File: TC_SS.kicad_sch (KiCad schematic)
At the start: 35 parts, among them Q1 C2M0025120D, Q2 C2M0025120D, Q3 C2M0025120D, Q4 C2M0025120D, U1 IR2184, U2 IR2184, U3 SN74LVC1G14DBV, U4 SN74LVC1G14DBV, U5 NE555D

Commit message: Add more values
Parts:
- D8, D9: value D -> 1n4148
- F1: value Fuse -> 10A
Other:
- moved on the sheet: AE1
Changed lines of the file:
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@@
     (stroke (width 0) (type default))
   )
-  (wire (pts (xy 118.11 166.37) (xy 109.22 166.37))
+  (wire (pts (xy 120.65 166.37) (xy 109.22 166.37))
     (stroke (width 0) (type default))
   )
@@
     (stroke (width 0) (type default))
   )
-  (wire (pts (xy 118.11 165.1) (xy 118.11 166.37))
+  (wire (pts (xy 120.65 165.1) (xy 120.65 166.37))
     (stroke (width 0) (type default))
   )
@@
       (effects (font (size 1.27 1.27)) (justify left))
     )
-    (property "Value" "D" (at 111.76 161.29 90)
+    (property "Value" "1n4148" (at 111.76 161.29 90)
       (effects (font (size 1.27 1.27)) (justify left))
     )
@@
       (effects (font (size 1.27 1.27)))
     )
-    (property "Value" "Fuse" (at 41.91 43.18 90)
+    (property "Value" "10A" (at 41.91 43.18 90)
       (effects (font (size 1.27 1.27)))
     )
@@
       (effects (font (size 1.27 1.27)) (justify left))
     )
-    (property "Value" "D" (at 111.76 173.99 90)
+    (property "Value" "1n4148" (at 111.76 173.99 90)
       (effects (font (size 1.27 1.27)) (justify left))
     )
@@
     )
   )
-  (symbol (lib_id "Device:Antenna") (at 118.11 160.02 0) (unit 1)
-    (in_bom yes) (on_board yes) (dnp no) (fields_autoplaced)
-    (property "Reference" "AE1" (at 120.65 159.385 0)
-      (effects (font (size 1.27 1.27)) (justify left))
-    )
-    (property "Value" "Antenna" (at 120.65 161.925 0)
-      (effects (font (size 1.27 1.27)) (justify left))
-    )
-    (property "Footprint" "" (at 118.11 160.02 0)
-      (effects (font (size 1.27 1.27)) hide)
-    )
-    (property "Datasheet" "~" (at 118.11 160.02 0)
-      (effects (font (size 1.27 1.27)) hide)
-    )
+  (symbol (lib_id "Device:Antenna") (at 120.65 160.02 0) (unit 1)
+    (in_bom yes) (on_board yes) (dnp no) (fields_autoplaced)
+    (property "Reference" "AE1" (at 123.19 159.385 0)
+      (effects (font (size 1.27 1.27)) (justify left))
+    )
+    (property "Value" "Antenna" (at 123.19 161.925 0)
+      (effects (font (size 1.27 1.27)) (justify left))
+    )
+    (property "Footprint" "" (at 120.65 160.02 0)
+      (effects (font (size 1.27 1.27)) hide)
+    )
+    (property "Datasheet" "~" (at 120.65 160.02 0)
+      (effects (font (size 1.27 1.27)) hide)
+    )

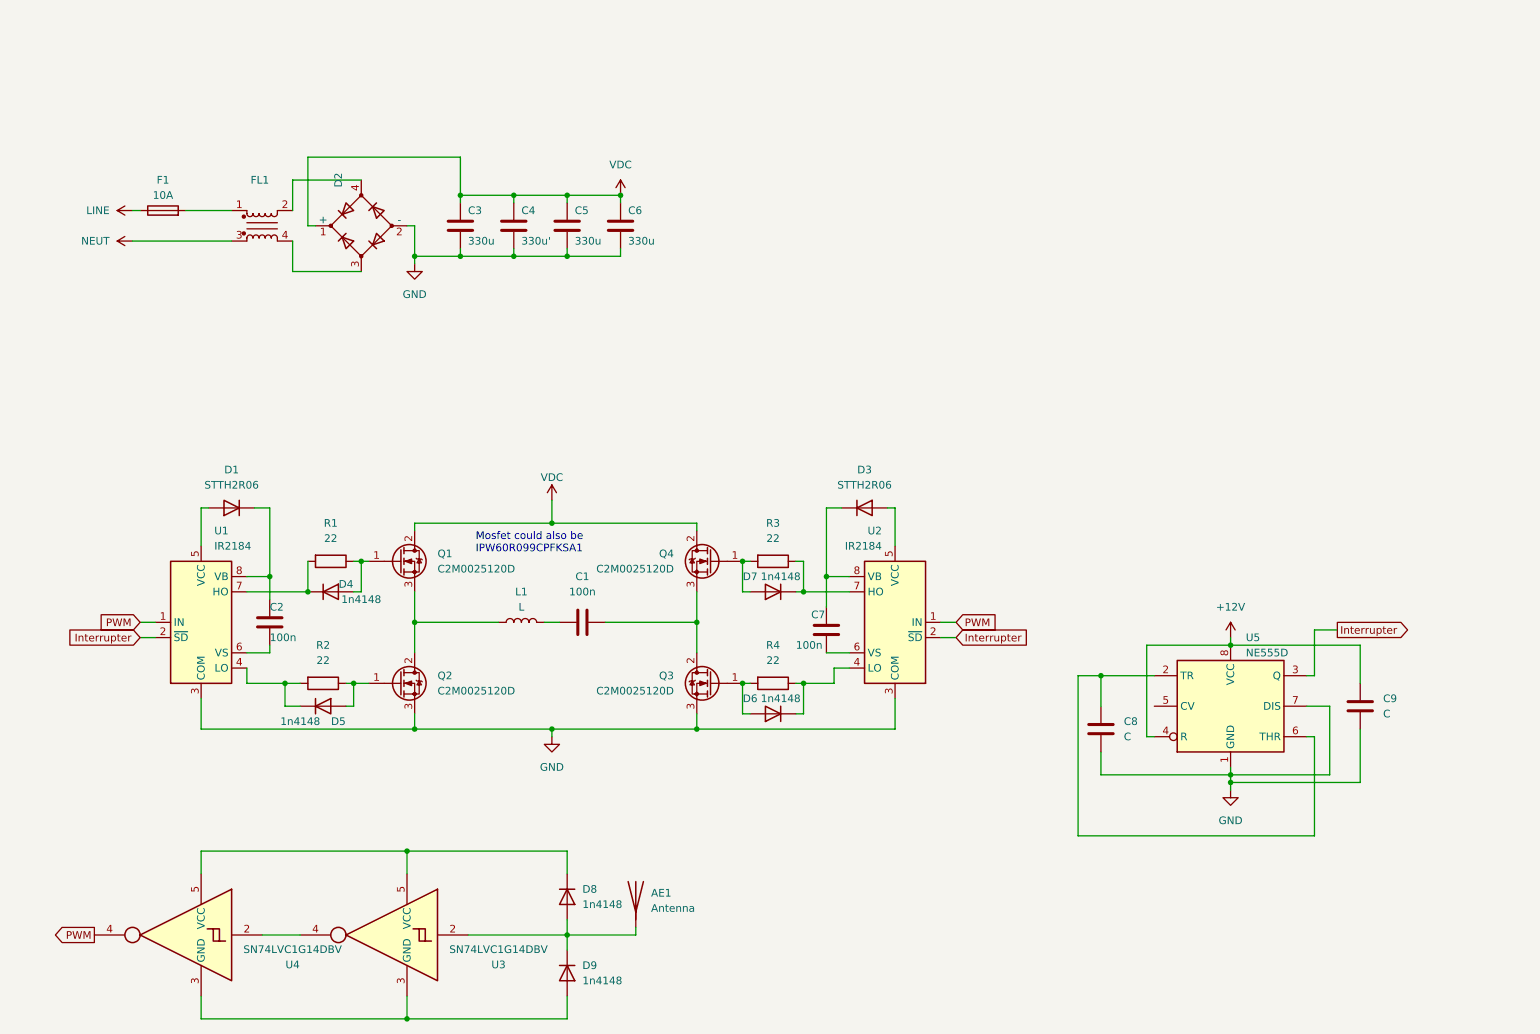
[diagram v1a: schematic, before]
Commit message: Update input driver
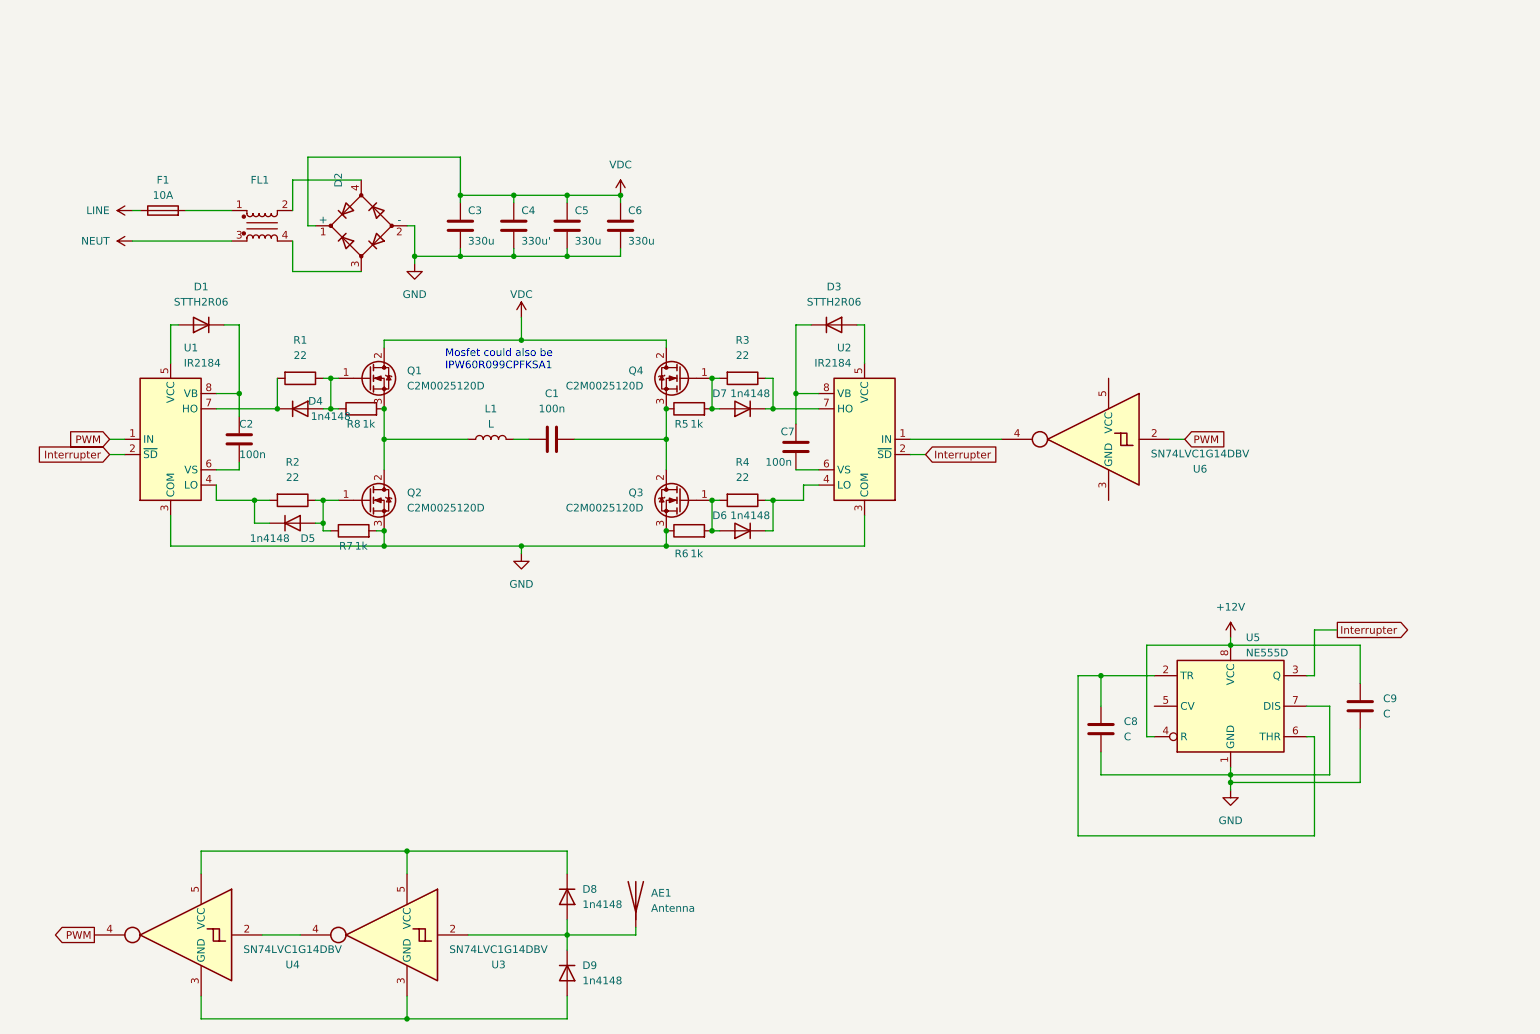
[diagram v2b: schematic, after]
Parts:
- added R5, R6, R7, R8: 1k, Resistor_SMD:R_1206_3216Metric_Pad1.30x1.75mm_HandSolder, symbol Device:R
- added U6: SN74LVC1G14DBV, Package_TO_SOT_SMD:SOT-23-5, symbol 74xGxx:SN74LVC1G14DBV
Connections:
- net GND: now also R6.1, R7.2
- net PWM: now also U6.2; no longer U2.1 (IN)
- net at D4.2 (A), Q1.1 (G), R1.1: now also R8.1
- net at L1.1, Q1.3 (S), Q2.2 (D): now also R8.2
- net at D5.2 (A), Q2.1 (G), R2.1: now also R7.1
- net at D6.2 (A), Q3.1 (G), R4.2: now also R6.2
- net at C1.2, Q3.2 (D), Q4.3 (S): now also R5.1
- net at D7.2 (A), Q4.1 (G), R3.2: now also R5.2
- new net: U2.1 (IN), U6.4
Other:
- moved on the sheet: C1, C2, C7, D1, D3, D4, D5, D6, D7, L1, Q1, Q2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

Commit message: Add more footprints and start board
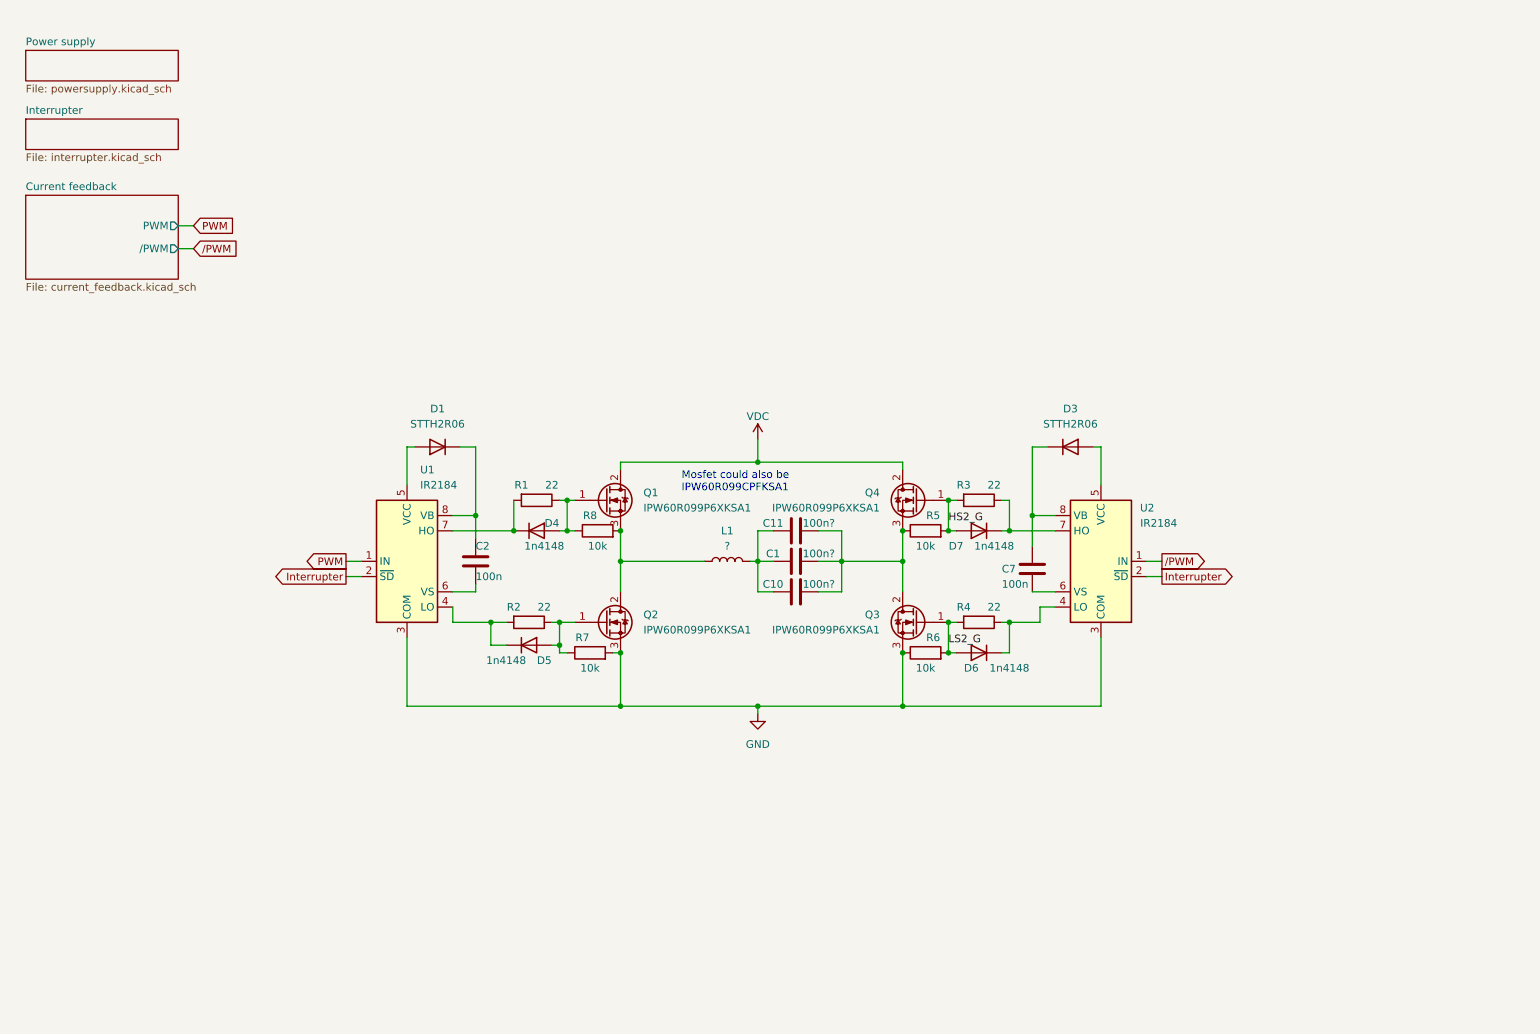
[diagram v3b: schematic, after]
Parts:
- removed AE1: Antenna, symbol Device:Antenna
- removed C3, C5, C6: 330u, Capacitor_SMD:C_0805_2012Metric_Pad1.18x1.45mm_HandSolder, symbol Device:C
- removed C4: 330u', Capacitor_SMD:C_0805_2012Metric_Pad1.18x1.45mm_HandSolder, symbol Device:C
- removed C8, C9: C, Capacitor_SMD:C_0805_2012Metric_Pad1.18x1.45mm_HandSolder, symbol Device:C
- removed D2: D_Bridge_+-AA, Diode_THT:Diode_Bridge_Vishay_KBPC6, symbol Device:D_Bridge_+-AA
- removed D8, D9: 1n4148, Diode_SMD:D_SMB, symbol Device:D
- removed F1: 10A, symbol Device:Fuse
- removed FL1: Filter_EMI_CommonMode, Inductor_THT:L_CommonMode_PulseElectronics_PH9455x155NL_1, symbol Device:Filter_EMI_CommonMode
- removed U3, U4, U6: SN74LVC1G14DBV, Package_TO_SOT_SMD:SOT-23-5, symbol 74xGxx:SN74LVC1G14DBV
- removed U5: NE555D, Package_SO:SOIC-8_3.9x4.9mm_P1.27mm, symbol Timer:NE555D
- added C10, C11: 100n?, Capacitor_SMD:C_2220_5750Metric, symbol Device:C
- C1: value 100n -> 100n?; footprint Capacitor_THT:C_Rect_L13.0mm_W3.0mm_P10.00mm_FKS3_FKP3_MKS4 -> Capacitor_SMD:C_2220_5750Metric
- L1: value L -> ?
- Q1, Q2, Q3, Q4: value C2M0025120D -> IPW60R099P6XKSA1
- R5, R6, R7, R8: value 1k -> 10k
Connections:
- net /PWM: now reaches U2.1 (IN)
- net at C1.1, L1.2: now also C10.1, C11.1
- net at C1.2, Q3.2 (D), Q4.3 (S)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: now also C10.2, C11.2
- net HS2_G: now reaches D7.2 (A), Q4.1 (G), R3.2, R5.2
- net LS2_G: now reaches D6.2 (A), Q3.1 (G), R4.2, R6.2
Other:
- added sheet Current feedback (current_feedback.kicad_sch)
- added sheet Interrupter (interrupter.kicad_sch)
- added sheet Power supply (powersupply.kicad_sch)
- moved on the sheet: C1, C2, C7, D1, D3, D4, D5, D6, D7, L1, Q1, Q2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

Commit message: Update Power PCB
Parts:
- added C12, C13, C14, C15, C16, C17, C18, C19: 100n?, Capacitor_SMD:C_2220_5650Metric, symbol Device:C
- added C20, C21: 100n, Capacitor_SMD:C_2220_5650Metric, symbol Device:C
- C1, C10, C11: value 100n? -> 100n; footprint Capacitor_SMD:C_2220_5750Metric -> Capacitor_SMD:C_2220_5650Metric
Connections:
- net GND: now also C12.2, C13.2, C14.2, C15.2, C16.2, C17.2, C18.2, C19.2
- net VDC: now also C12.1, C13.1, C14.1, C15.1, C16.1, C17.1, C18.1, C19.1
- net HS1_G: now reaches D4.2 (A), Q1.1 (G), R1.1, R8.1
- net HB1: now reaches L1.1, Q1.3 (S), Q2.2 (D), R8.2
- net at C1.1, C10.1, C11.1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: now also C20.1, C21.1
- net HB2: now reaches C1.2, C10.2, C11.2, Q3.2 (D), Q4.3 (S), R5.1
- net HB2: now also C20.2, C21.2
- net LS1_G: now reaches D5.2 (A), Q2.1 (G), R2.1, R7.1

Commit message: Do power PCB layout
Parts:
- C12, C13, C14, C15, C16, C17, C18, C19: value 100n? -> 100n
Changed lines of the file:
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@@
       (effects (font (size 1.27 1.27)))
     )
-    (property "Value" "100n?" (at 153.67 80.01 90)
+    (property "Value" "100n" (at 153.67 80.01 90)
       (effects (font (size 1.27 1.27)))
     )
@@
       (effects (font (size 1.27 1.27)))
     )
-    (property "Value" "100n?" (at 163.83 80.01 90)
+    (property "Value" "100n" (at 163.83 80.01 90)
       (effects (font (size 1.27 1.27)))
     )
@@
       (effects (font (size 1.27 1.27)))
     )
-    (property "Value" "100n?" (at 127 80.01 90)
+    (property "Value" "100n" (at 127 80.01 90)
       (effects (font (size 1.27 1.27)))
     )
@@
       (effects (font (size 1.27 1.27)))
     )
-    (property "Value" "100n?" (at 158.75 80.01 90)
+    (property "Value" "100n" (at 158.75 80.01 90)
       (effects (font (size 1.27 1.27)))
     )
@@
       (effects (font (size 1.27 1.27)))
     )
-    (property "Value" "100n?" (at 121.92 80.01 90)
+    (property "Value" "100n" (at 121.92 80.01 90)
       (effects (font (size 1.27 1.27)))
     )
@@
       (effects (font (size 1.27 1.27)))
     )
-    (property "Value" "100n?" (at 148.59 80.01 90)
+    (property "Value" "100n" (at 148.59 80.01 90)
       (effects (font (size 1.27 1.27)))
     )
@@
       (effects (font (size 1.27 1.27)))
     )
-    (property "Value" "100n?" (at 116.84 80.01 90)
+    (property "Value" "100n" (at 116.84 80.01 90)
       (effects (font (size 1.27 1.27)))
     )
@@
       (effects (font (size 1.27 1.27)))
     )
-    (property "Value" "100n?" (at 132.08 80.01 90)
-      (effects (font (size 1.27 1.27)))
-    )
+    (property "Value" "100n" (at 132.08 80.01 90)
+      (effects (font (size 1.27 1.27)))
+    )

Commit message: Update schematic
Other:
- removed sheet Current feedback
- removed sheet Interrupter
- removed sheet Power supply
- note removed: "Mosfet could also be IPW60R099CPFKSA1"
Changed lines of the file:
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@@
-    (stroke (width 0) (type default))
-  )
-  (wire (pts (xy 44.45 52.07) (xy 46.99 52.07))
     (stroke (width 0) (type default))
   )
@@
     (stroke (width 0) (type default))
   )
-  (wire (pts (xy 44.45 48.26) (xy 46.99 48.26))
-    (stroke (width 0) (type default))
-  )
   (wire (pts (xy 173.99 99.06) (xy 172.72 99.06))
     (stroke (width 0) (type default))
@@
   (wire (pts (xy 106.68 114.3) (xy 107.95 114.3))
     (stroke (width 0) (type default))
-  )
-  (text "Mosfet could also be \nIPW60R099CPFKSA1" (at 128.27 92.71 0)
-    (effects (font (size 1.27 1.27)) (justify left bottom))
   )
   (label "LS1_G" (at 107.95 114.3 0) (fields_autoplaced)
@@
   (label "HS2_G" (at 172.72 97.79 0) (fields_autoplaced)
     (effects (font (size 1.27 1.27)) (justify left bottom))
-  )
-  (global_label "PWM" (shape input) (at 46.99 48.26 0) (fields_autoplaced)
-    (effects (font (size 1.27 1.27)) (justify left))
-    (property "Intersheetrefs" "${INTERSHEET_REFS}" (at 54.148 48.26 0)
-      (effects (font (size 1.27 1.27)) (justify left) hide)
-    )
   )
   (global_label "{slash}PWM" (shape output) (at 208.28 104.14 0) (fields_autoplaced)
@@
     (property "Intersheetrefs" "${INTERSHEET_REFS}" (at 59.3658 106.68 0)
       (effects (font (size 1.27 1.27)) (justify right) hide)
-    )
-  )
-  (global_label "{slash}PWM" (shape input) (at 46.99 52.07 0) (fields_autoplaced)
-    (effects (font (size 1.27 1.27)) (justify left))
-    (property "Intersheetrefs" "${INTERSHEET_REFS}" (at 55.4785 52.07 0)
-      (effects (font (size 1.27 1.27)) (justify left) hide)
     )
   )
@@
       )
     )
-  )
-  (sheet (at 19.05 43.18) (size 25.4 13.97) (fields_autoplaced)
-    (stroke (width 0.1524) (type solid))
-    (fill (color 0 0 0 0.0000))
-    (property "Sheetname" "Current feedback" (at 19.05 42.4684 0)
-      (effects (font (size 1.27 1.27)) (justify left bottom))
-    )
-    (property "Sheetfile" "current_feedback.kicad_sch" (at 19.05 57.7346 0)
-      (effects (font (size 1.27 1.27)) (justify left top))
-    )
-    (pin "PWM" output (at 44.45 48.26 0)
-      (effects (font (size 1.27 1.27)) (justify right))
-    )
-    (pin "{slash}PWM" output (at 44.45 52.07 0)
-      (effects (font (size 1.27 1.27)) (justify right))
-    )
-    (instances
-      (project "TC_SS"
-        (path "/3ea854a4-6c65-43a0-a0e2-a46500cc93c9" (page "2"))
-      )
-    )
-  )
-  (sheet (at 19.05 19.05) (size 25.4 5.08) (fields_autoplaced)
-    (stroke (width 0.1524) (type solid))
-    (fill (color 0 0 0 0.0000))
-    (property "Sheetname" "Power supply" (at 19.05 18.3384 0)
-      (effects (font (size 1.27 1.27)) (justify left bottom))
-    )
-    (property "Sheetfile" "powersupply.kicad_sch" (at 19.05 24.7146 0)
-      (effects (font (size 1.27 1.27)) (justify left top))
-    )
-    (instances
-      (project "TC_SS"
-        (path "/3ea854a4-6c65-43a0-a0e2-a46500cc93c9" (page "3"))
-      )
-    )
-  )
-  (sheet (at 19.05 30.48) (size 25.4 5.08) (fields_autoplaced)
-    (stroke (width 0.1524) (type solid))
-    (fill (color 0 0 0 0.0000))
-    (property "Sheetname" "Interrupter" (at 19.05 29.7684 0)
-      (effects (font (size 1.27 1.27)) (justify left bottom))
-    )
-    (property "Sheetfile" "interrupter.kicad_sch" (at 19.05 36.1446 0)
-      (effects (font (size 1.27 1.27)) (justify left top))
-    )
-    (property "Felt 2" "" (at 19.05 30.48 0)
-      (effects (font (size 1.27 1.27)) hide)
-    )
-    (instances
-      (project "TC_SS"
-        (path "/3ea854a4-6c65-43a0-a0e2-a46500cc93c9" (page "4"))
-      )
-    )
